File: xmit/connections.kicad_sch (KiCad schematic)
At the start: 9 parts, among them J1 Conn_Coaxial, J2 Conn_01x02, J4 Conn_01x02, J5 Conn_01x02, J6 Conn_01x02

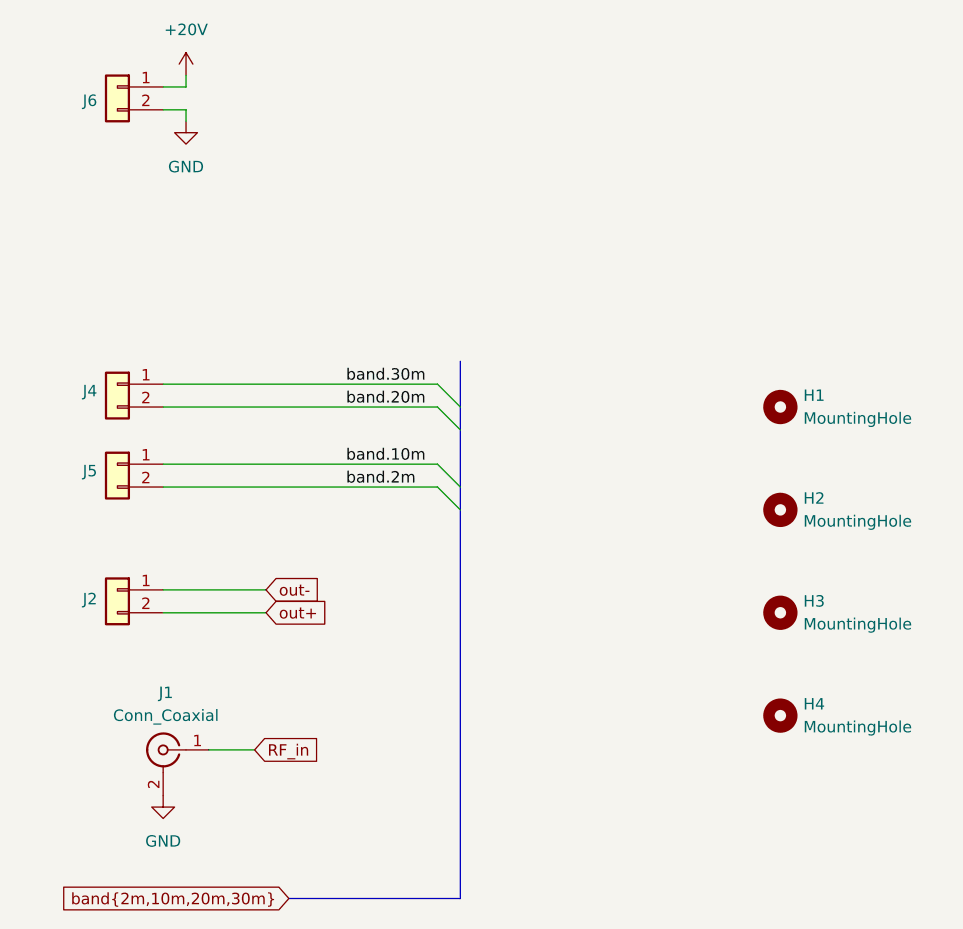
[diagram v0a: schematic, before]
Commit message: More layout cleanup.
This is a checkpoint before I move all of the power management to a separate board. Next step is to move all power management to a separate board.
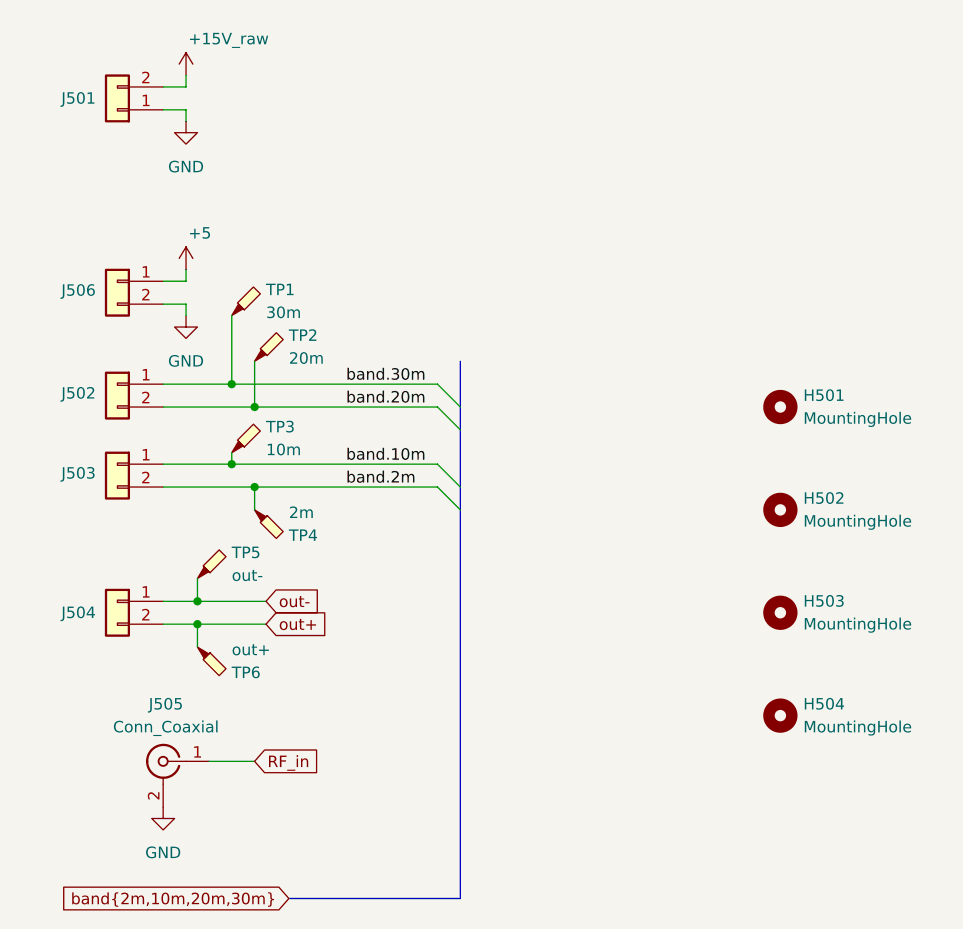
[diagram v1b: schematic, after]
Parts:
- removed J6: Conn_01x02, Connector:terminal_block_02, symbol Connector_Generic:Conn_01x02
- added J501, J506: Conn_01x02, Connector:terminal_block_02, symbol Connector_Generic:Conn_01x02
- added TP1: 30m, TestPoint:TestPoint_Pad_1.0x1.0mm, symbol Connector:TestPoint_Probe
- added TP2: 20m, TestPoint:TestPoint_Pad_1.0x1.0mm, symbol Connector:TestPoint_Probe
- added TP3: 10m, TestPoint:TestPoint_Pad_1.0x1.0mm, symbol Connector:TestPoint_Probe
- added TP4: 2m, TestPoint:TestPoint_Pad_1.0x1.0mm, symbol Connector:TestPoint_Probe
- added TP5: out-, TestPoint:TestPoint_2Pads_Pitch2.54mm_Drill0.8mm, symbol Connector:TestPoint_Probe
- added TP6: out+, TestPoint:TestPoint_2Pads_Pitch2.54mm_Drill0.8mm, symbol Connector:TestPoint_Probe
- renumbered H1 to H501, H2 to H502, H3 to H503, H4 to H504, J4 to J502, J5 to J503, J2 to J504, J1 to J505
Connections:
- net GND: now also J501.1 (Pin_1), J506.2 (Pin_2)
- net band.10m: now also TP3.1
- net band.20m: now also TP2.1
- net band.2m: now also TP4.1
- net band.30m: now also TP1.1
- net out+: now also TP6.1
- net out-: now also TP5.1
- new net +15V_raw: J501.2 (Pin_2)
- new net +5: J506.1 (Pin_1)
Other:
- moved on the sheet: J504, J505

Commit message: changes up to first spin
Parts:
- removed TP1: 30m, TestPoint:TestPoint_Pad_1.0x1.0mm, symbol Connector:TestPoint_Probe
- removed TP2: 20m, TestPoint:TestPoint_Pad_1.0x1.0mm, symbol Connector:TestPoint_Probe
- removed TP3: 10m, TestPoint:TestPoint_Pad_1.0x1.0mm, symbol Connector:TestPoint_Probe
- removed TP4: 2m, TestPoint:TestPoint_Pad_1.0x1.0mm, symbol Connector:TestPoint_Probe
- H501, H502, H503, H504: value MountingHole -> (none); KiLib_Generator (none) -> mounting_hardware/mounting_hole
- J501: value Conn_01x02 -> (none); footprint Connector:terminal_block_02 -> TerminalBlock_TE-Connectivity:TerminalBlock_TE_282834-2_1x02_P2.54mm_Horizontal; symbol Connector_Generic:Conn_01x02 -> Connector:Screw_Terminal_01x02; KiLib_Generator (none) -> terminal_block/TE_Connectivity; now left out of the parts list
- J502: renamed from J506; value Conn_01x02 -> (none); footprint Connector:terminal_block_02 -> TerminalBlock_TE-Connectivity:TerminalBlock_TE_282834-2_1x02_P2.54mm_Horizontal; symbol Connector_Generic:Conn_01x02 -> Connector:Screw_Terminal_01x02; KiLib_Generator (none) -> terminal_block/TE_Connectivity; now left out of the parts list
- J503: renamed from J502; value Conn_01x02 -> (none); footprint Connector:terminal_block_02 -> TerminalBlock_TE-Connectivity:TerminalBlock_TE_282834-2_1x02_P2.54mm_Horizontal; symbol Connector_Generic:Conn_01x02 -> Connector:Screw_Terminal_01x02; KiLib_Generator (none) -> terminal_block/TE_Connectivity; now left out of the parts list
- J504: renamed from J503; value Conn_01x02 -> (none); footprint Connector:terminal_block_02 -> TerminalBlock_TE-Connectivity:TerminalBlock_TE_282834-2_1x02_P2.54mm_Horizontal; symbol Connector_Generic:Conn_01x02 -> Connector:Screw_Terminal_01x02; KiLib_Generator (none) -> terminal_block/TE_Connectivity; now left out of the parts list
- J505: renamed from J504; value Conn_01x02 -> (none); footprint Connector:terminal_block_02 -> TerminalBlock_TE-Connectivity:TerminalBlock_TE_282834-2_1x02_P2.54mm_Horizontal; symbol Connector_Generic:Conn_01x02 -> Connector:Screw_Terminal_01x02; KiLib_Generator (none) -> terminal_block/TE_Connectivity; now left out of the parts list
- J506: renamed from J505; value Conn_Coaxial -> (none); LCSC Part # (none) -> C49118400; now left out of the parts list
- TP501: renamed from TP5; value out- -> (none); LCSC Part # (none) -> C45367201; now left out of the parts list
- TP502: renamed from TP6; value out+ -> (none); LCSC Part # (none) -> C113518; now left out of the parts list
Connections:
- net +5 renamed +5V_raw
